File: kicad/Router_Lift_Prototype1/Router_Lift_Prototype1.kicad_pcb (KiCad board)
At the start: 2 copper layers, 31 parts, among them J1 Conn_01x02, J10 Conn_01x02, J11 Conn_01x04, J2 Conn_01x02, J3 Conn_01x06, J4 Conn_01x06, J5 Conn_01x06, J6 Conn_01x02, J7 Conn_01x02, J8 Conn_01x02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

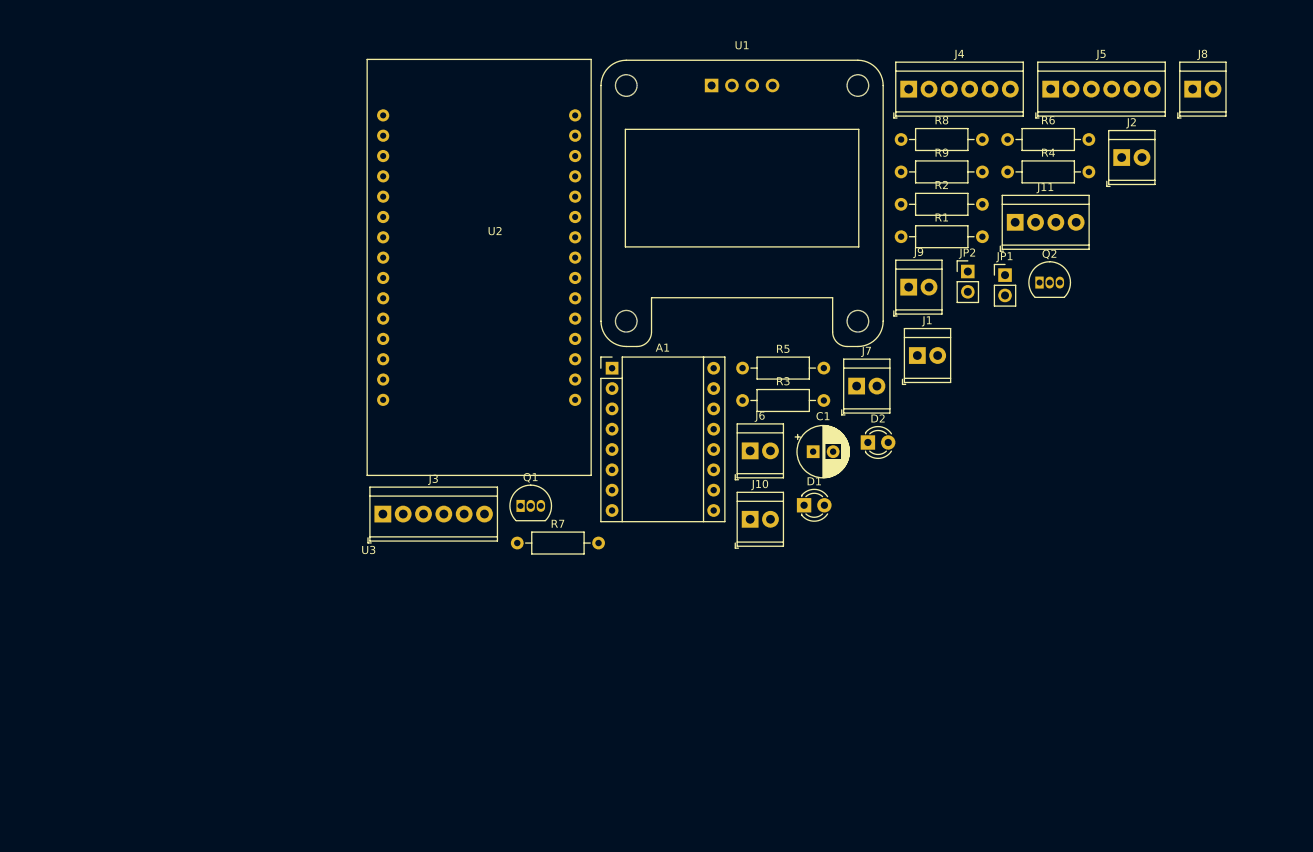
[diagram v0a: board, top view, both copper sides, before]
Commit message: Component placement and start routing test
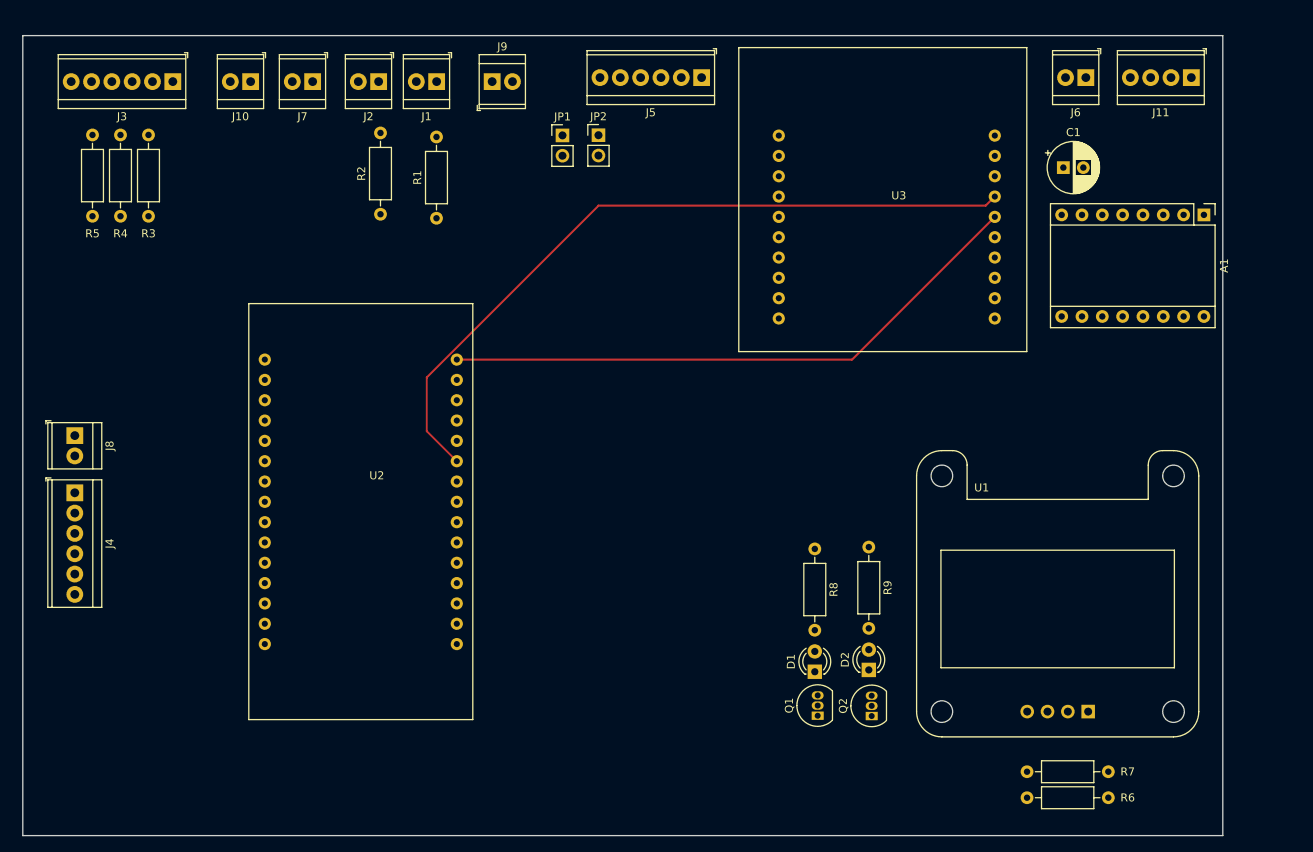
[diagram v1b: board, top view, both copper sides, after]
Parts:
- moved J8 146.3 mm to (57.3, 102.4), turned to -90 degrees
- moved J4 115.8 mm to (57.3, 109.5), turned to -90 degrees
- moved R4 111.0 mm to (63.0, 75.0), turned to 90 degrees
- moved U1 97.0 mm to (189.1, 136.9), turned to 180 degrees
- moved J2 93.4 mm to (95.3, 58.1), turned to 180 degrees
- moved R5 83.4 mm to (59.5, 75.0), turned to 90 degrees
- moved R6 83.2 mm to (186.5, 147.7), turned to 180 degrees
- moved J10 83.0 mm to (79.3, 58.1), turned to 180 degrees
- moved U3 79.7 mm to (160.3, 72.9)
- moved R7 79.2 mm to (186.5, 144.4), turned to 180 degrees
- moved J7 77.9 mm to (87.0, 58.1), turned to 180 degrees
- moved R3 77.7 mm to (66.5, 75.0), turned to 90 degrees
- moved A1 76.4 mm to (198.4, 74.8), turned to -90 degrees
- moved J1 69.2 mm to (102.5, 58.1), turned to 180 degrees
- moved R2 65.1 mm to (95.5, 74.7), turned to 90 degrees
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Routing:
- net /MISO: track 0.00 -> 92.4 mm
- net /MOSI: track 0.00 -> 74.6 mm
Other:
- board outline added: 150 x 100 mm

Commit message: Further placement
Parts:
- added REF**: MountingHole_3.2mm_M3_ISO7380, MountingHole:MountingHole_3.2mm_M3_ISO7380, F.Cu at (55.0, 55.0)
- added REF**: MountingHole_3.2mm_M3_ISO7380, MountingHole:MountingHole_3.2mm_M3_ISO7380, F.Cu at (205.0, 55.0)
- added REF**: MountingHole_3.2mm_M3_ISO7380, MountingHole:MountingHole_3.2mm_M3_ISO7380, F.Cu at (205.0, 145.0)
- added REF**: MountingHole_3.2mm_M3_ISO7380, MountingHole:MountingHole_3.2mm_M3_ISO7380, F.Cu at (55.0, 145.0)
- moved R4 5.65 mm to (68.1, 72.6)
- moved R5 5.65 mm to (64.6, 72.6)
- moved R1 5.65 mm to (107.6, 72.8)
- moved R2 5.65 mm to (100.6, 72.3)
- moved R3 5.65 mm to (71.6, 72.6)
- moved J1 5.65 mm to (107.6, 55.7)
- moved J10 5.65 mm to (84.4, 55.7)
- moved J2 5.65 mm to (100.4, 55.7)
- moved J3 5.65 mm to (74.7, 55.7)
- moved J7 5.65 mm to (92.1, 55.7)
- moved Q2 4.33 mm to (160.5, 135.0)
- moved J8 4.33 mm to (60.9, 100.0)
- moved U2 4.33 mm to (96.6, 109.5)
- moved J9 4.33 mm to (113.1, 55.7)
- moved J4 4.33 mm to (60.9, 107.1)
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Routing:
- net /MISO: track 92.4 -> 86.6 mm
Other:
- board size 150 x 100 mm -> 160 x 100 mm

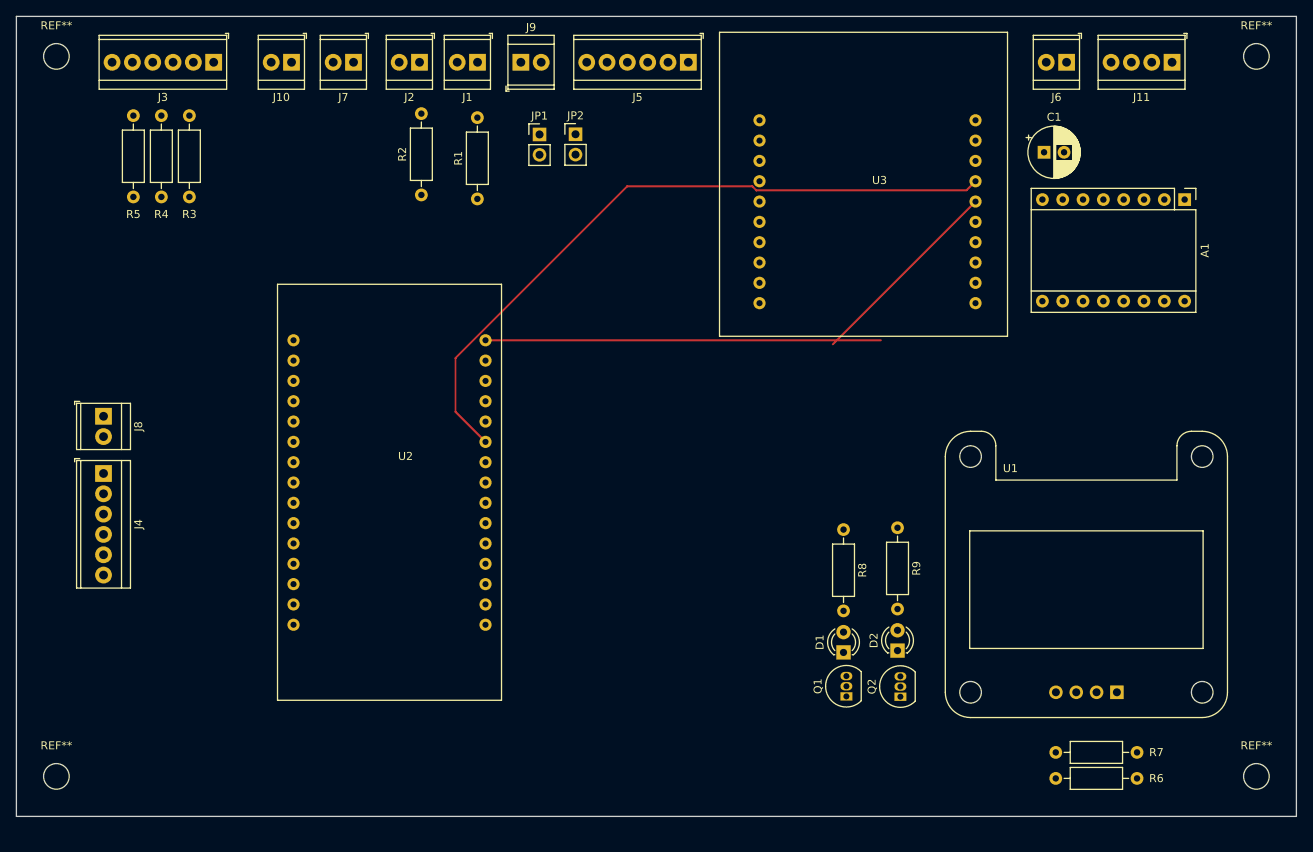
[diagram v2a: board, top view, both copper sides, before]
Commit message: Completing Layout - Several Pin changes to be updated in Software
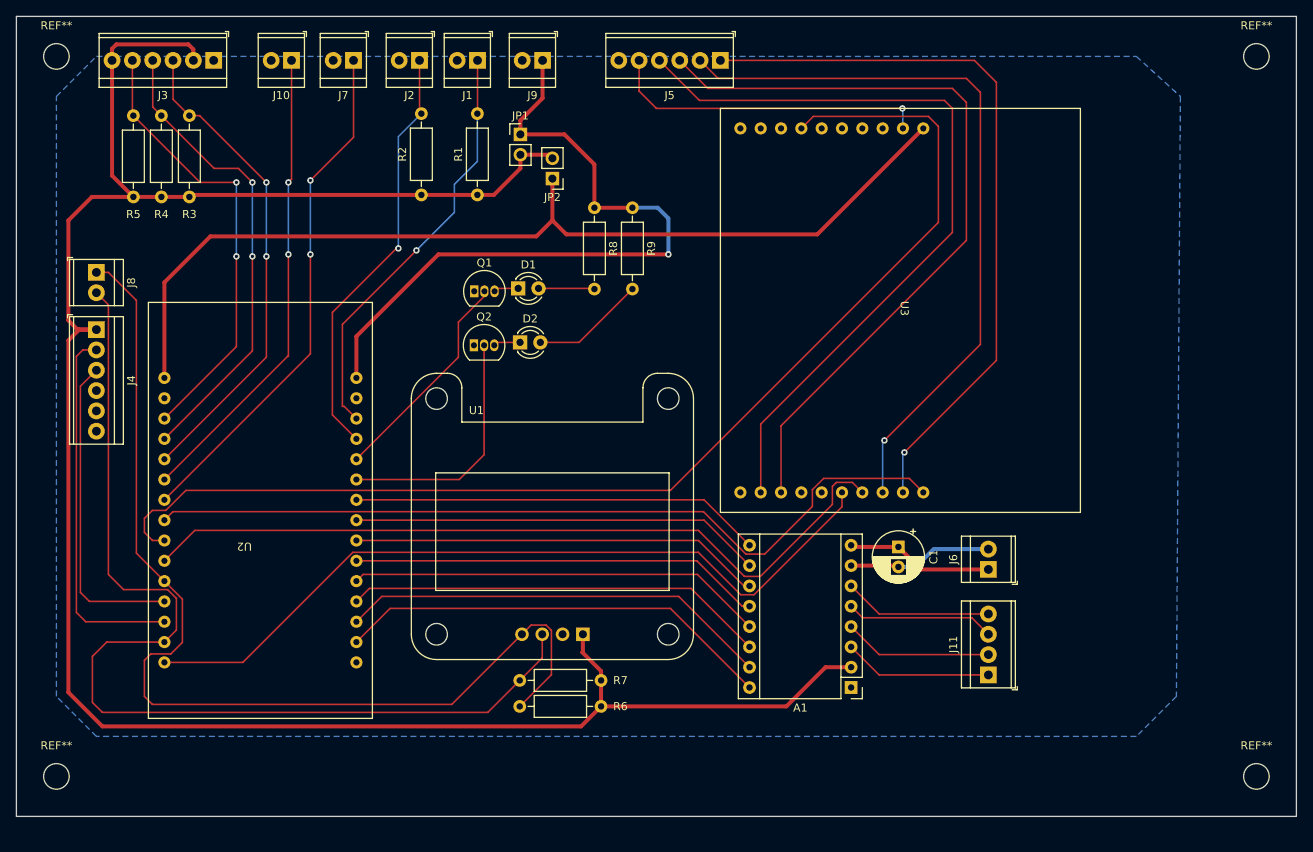
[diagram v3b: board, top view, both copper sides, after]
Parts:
- moved J11 79.9 mm to (171.5, 132.3), turned to 90 degrees
- moved A1 73.9 mm to (154.3, 133.9), turned to 180 degrees
- moved Q2 69.1 mm to (107.2, 91.1), turned to 0 degrees
- moved Q1 68.8 mm to (107.2, 84.4), turned to 0 degrees
- moved R6 67.6 mm to (123.1, 136.2)
- moved R7 67.6 mm to (123.1, 133.0)
- moved U1 67.1 mm to (125.9, 127.2)
- moved J6 64.1 mm to (171.5, 119.1), turned to 90 degrees
- moved D1 61.0 mm to (112.7, 84.0), turned to 0 degrees
- moved D2 60.9 mm to (113.0, 90.8), turned to 0 degrees
- moved C1 52.6 mm to (160.2, 116.3), turned to -90 degrees
- moved R9 51.9 mm to (127.0, 73.9)
- moved R8 50.9 mm to (122.2, 73.9)
- moved J4 18.0 mm to (60.0, 89.2)
- moved J8 18.0 mm to (60.0, 82.0)
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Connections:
- J5 pad 1: /~{STALL} -> /BIN2
- J5 pad 2: /~{FAULT} -> /BIN1
- J5 pad 3: /POT -> /~{FAULT}
- J5 pad 4: /BIN1 -> /~{STALL}
- J5 pad 5: /BIN2 -> /POT
- U2 pad 10: /BUTTON_A -> /LED_GREEN
- U2 pad 11: unconnected-(U2-Pad11) -> /LED_RED
- U2 pad 12: /STEP -> /ENDSWITCH_DOWN
- U2 pad 13: /DIR -> /ENDSWITCH_UP
- U2 pad 18: /LED_RED -> /ENC_A
- U2 pad 19: /~{ENABLE} -> /ENC_B
- U2 pad 2: /ENDSWITCH_UP -> /DIR
- U2 pad 20: /LED_GREEN -> /ENC_BUTTON
- U2 pad 21: /SLEEP -> /BUTTON_B
- U2 pad 22: /RESET -> /BUTTON_A
- U2 pad 3: /ENDSWITCH_DOWN -> /STEP
- U2 pad 4: /ENC_BUTTON -> /SLEEP
- U2 pad 5: /ENC_A -> /RESET
- U2 pad 6: /ENC_B -> /MS3
- U2 pad 7: /MS1 -> /MS2
- U2 pad 8: /MS2 -> /MS1
- U2 pad 9: /MS3 -> /~{ENABLE}
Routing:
- net VCC: track 0.00 -> 273.9 mm
- net /CLK: track 0.00 -> 149.5 mm
- net /SCK: track 0.00 -> 130.0 mm
- net /SDA: track 0.00 -> 128.6 mm
- net +3V3: track 0.00 -> 121.4 mm
- net /CS0: track 0.00 -> 103.4 mm
- net /~{STALL}: track 0.00 -> 97.0 mm
- net /~{FAULT}: track 0.00 -> 96.4 mm
- net /BIN1: track 0.00 -> 91.8 mm, vias 0 -> 1
- net /BIN2: track 0.00 -> 91.7 mm, vias 0 -> 1
- net +5V: track 0.00 -> 89.4 mm, vias 0 -> 1
- net /BUTTON_A: track 0.00 -> 64.7 mm, vias 0 -> 2
- net /ENC_BUTTON: track 0.00 -> 60.7 mm, vias 0 -> 2
- net /BUTTON_B: track 0.00 -> 59.3 mm, vias 0 -> 2
- net /ENC_B: track 0.00 -> 58.8 mm, vias 0 -> 2
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- added copper zone on B.Cu, net GND

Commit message: Finished routing before curving tracks and review
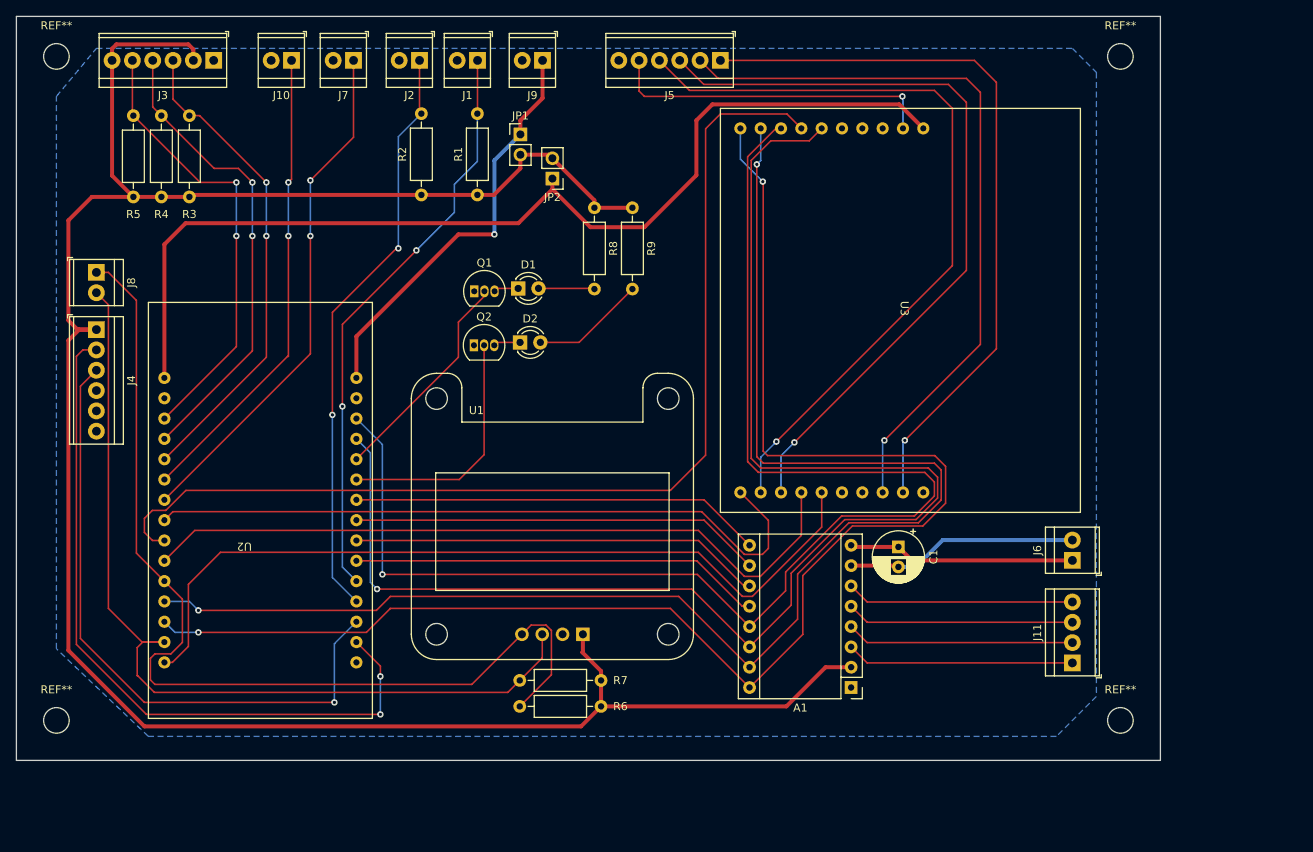
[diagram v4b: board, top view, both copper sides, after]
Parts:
- moved REF** 18.4 mm to (188.0, 138.0)
- moved REF** 17.0 mm to (188.0, 55.0)
- moved J11 10.6 mm to (182.0, 130.8)
- moved J6 10.6 mm to (182.0, 118.0)
- moved REF** 7.00 mm to (55.0, 138.0)
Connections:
- J5 pad 1: /BIN2 -> /~{STALL}
- J5 pad 2: /BIN1 -> /~{FAULT}
- J5 pad 3: /~{FAULT} -> /BIN1
- J5 pad 4: /~{STALL} -> /BIN2
- R8 pad 1: +5V -> VCC
- R9 pad 1: +5V -> VCC
- U2 pad 12: /ENDSWITCH_DOWN -> /SLEEP
- U2 pad 13: /ENDSWITCH_UP -> /RESET
- U2 pad 2: /DIR -> /TX0
- U2 pad 27: /RX0 -> /STEP
- U2 pad 28: /TX0 -> /DIR
- U2 pad 3: /STEP -> /RX0
- U2 pad 4: /SLEEP -> /ENDSWITCH_DOWN
- U2 pad 5: /RESET -> /ENDSWITCH_UP
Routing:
- net /DIR: track 55.0 -> 187.2 mm, vias 0 -> 2
- net /STEP: track 54.1 -> 182.6 mm, vias 0 -> 2
- net /SLEEP: track 52.8 -> 177.5 mm, vias 0 -> 1
- net /RESET: track 52.2 -> 170.6 mm, vias 0 -> 1
- net /TX0: track 46.3 -> 90.7 mm, vias 0 -> 2
- net /RX0: track 39.6 -> 80.6 mm, vias 0 -> 1
- net +5V: track 89.4 -> 52.0 mm
- net /ENDSWITCH_DOWN: track 53.4 -> 73.7 mm, vias 1 -> 2
- net /ENDSWITCH_UP: track 53.1 -> 72.9 mm, vias 1 -> 2
- net /SCK: track 130.0 -> 112.3 mm
- net /CLK: track 149.5 -> 132.4 mm
- net /CS0: track 103.4 -> 86.9 mm
- net GNDPWR: track 18.2 -> 29.1 mm
- net VCC: track 273.9 -> 284.0 mm
- net +VDC: track 18.4 -> 28.4 mm
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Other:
- board size 160 x 100 mm -> 143 x 93 mm

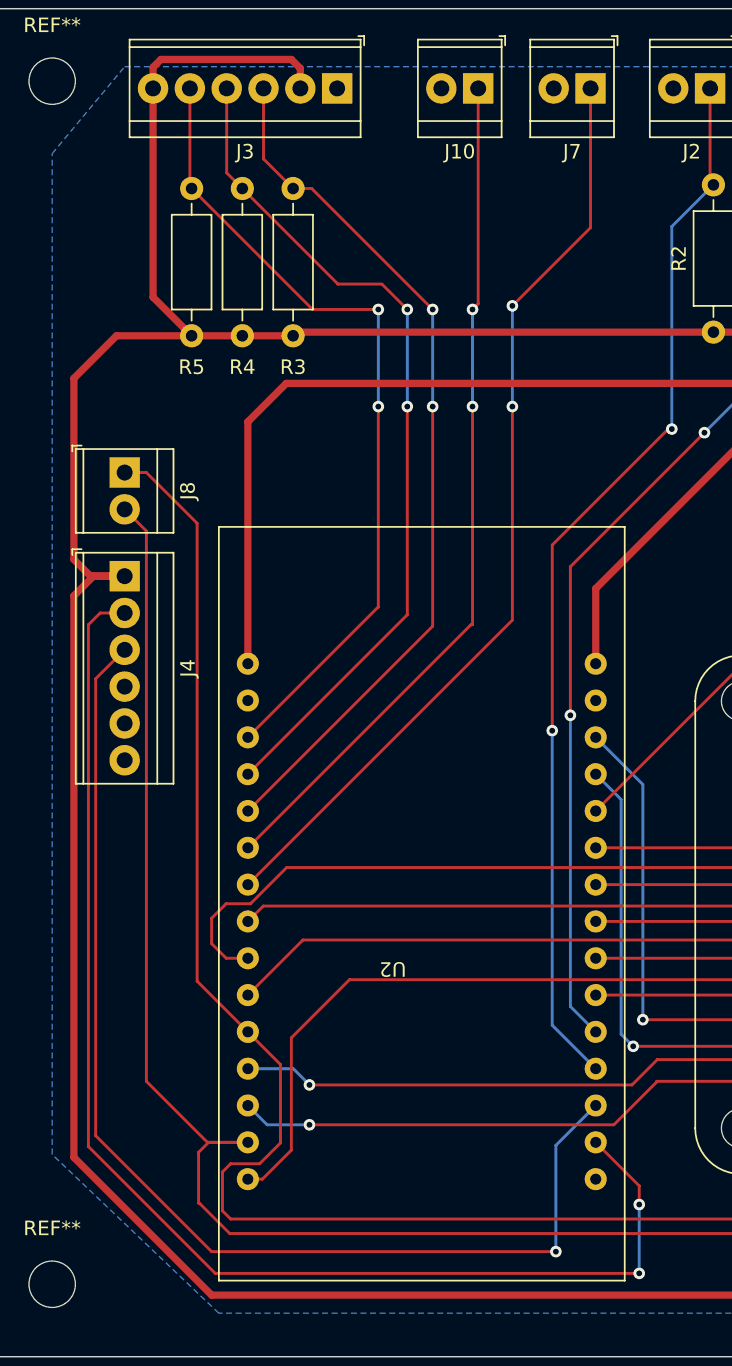
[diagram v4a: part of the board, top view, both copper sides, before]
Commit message: Updated changes in the PCB to include SPI changes
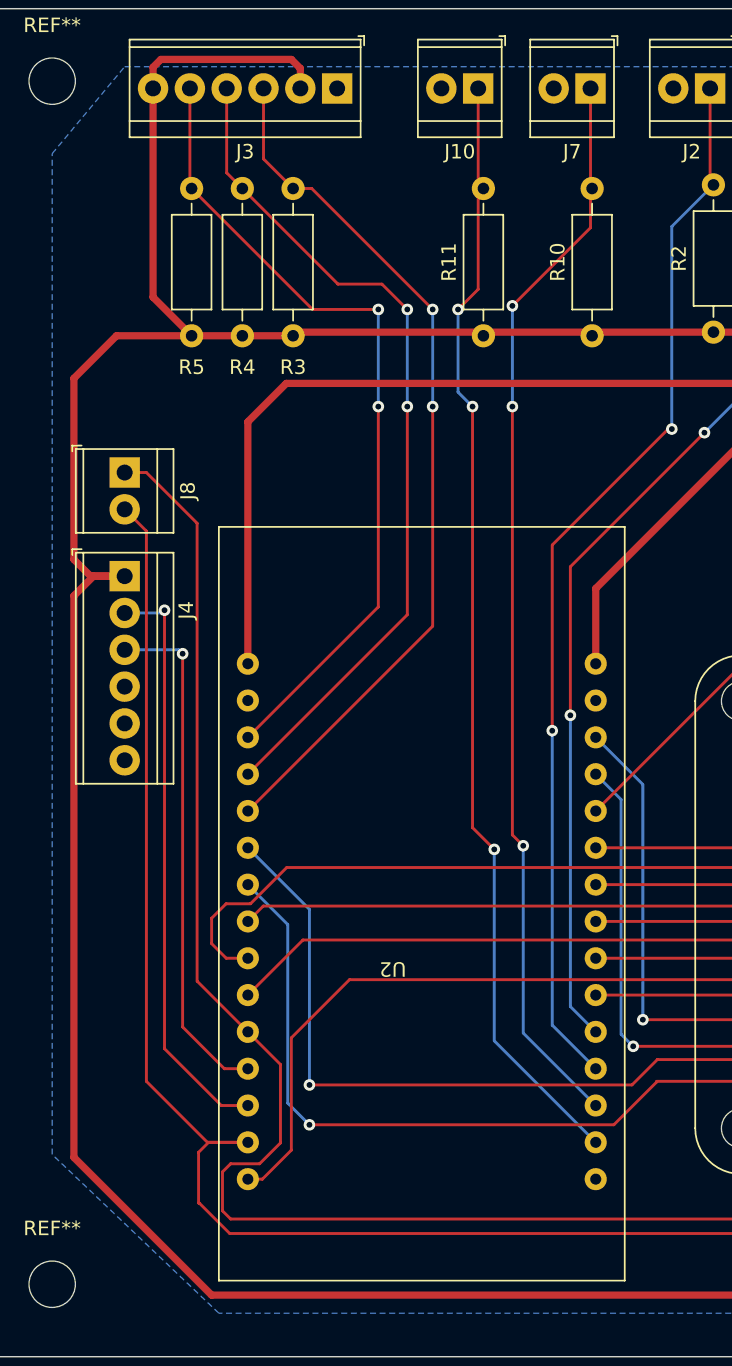
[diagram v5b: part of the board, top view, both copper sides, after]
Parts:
- added R10: R, Resistor_THT:R_Axial_DIN0207_L6.3mm_D2.5mm_P10.16mm_Horizontal, F.Cu at (92.2, 72.6)
- added R11: R, Resistor_THT:R_Axial_DIN0207_L6.3mm_D2.5mm_P10.16mm_Horizontal, F.Cu at (84.8, 72.6)
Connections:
- U2 pad 2: /TX0 -> /BUTTON_B
- U2 pad 21: /BUTTON_B -> /STEP
- U2 pad 22: /BUTTON_A -> /DIR
- U2 pad 27: /STEP -> /RX0
- U2 pad 28: /DIR -> /TX0
- U2 pad 3: /RX0 -> /BUTTON_A
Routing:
- net /TX0: track 90.7 -> 40.5 mm, vias 2 -> 1
- net /RX0: track 80.6 -> 35.6 mm
- net /BUTTON_B: track 59.0 -> 77.2 mm, vias 2 -> 3
- net /DIR: track 187.2 -> 200.8 mm
- net /STEP: track 182.6 -> 196.1 mm
- net /BUTTON_A: track 64.7 -> 74.8 mm, vias 2 -> 3
